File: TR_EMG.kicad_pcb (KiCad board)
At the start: 4 copper layers, 127 x 101.6 mm, 118 parts, among them J1 1727230, J2 1727230, J3 1844236, J4 MJ-3523-SMT-TR, J5 MJ-3523-SMT-TR, J6 MJ-3523-SMT-TR, J7 MJ-3523-SMT-TR, U1 ADS1115IDGSR, U101 INA115BU, U111 LT1169CS8-PBF, U112 LT1169CS8-PBF, U201 INA115BU, U211 LT1169CS8-PBF, U212 LT1169CS8-PBF, U301 INA115BU, U311 LT1169CS8-PBF, U312 LT1169CS8-PBF, U401 INA115BU, U411 LT1169CS8-PBF, U412 LT1169CS8-PBF

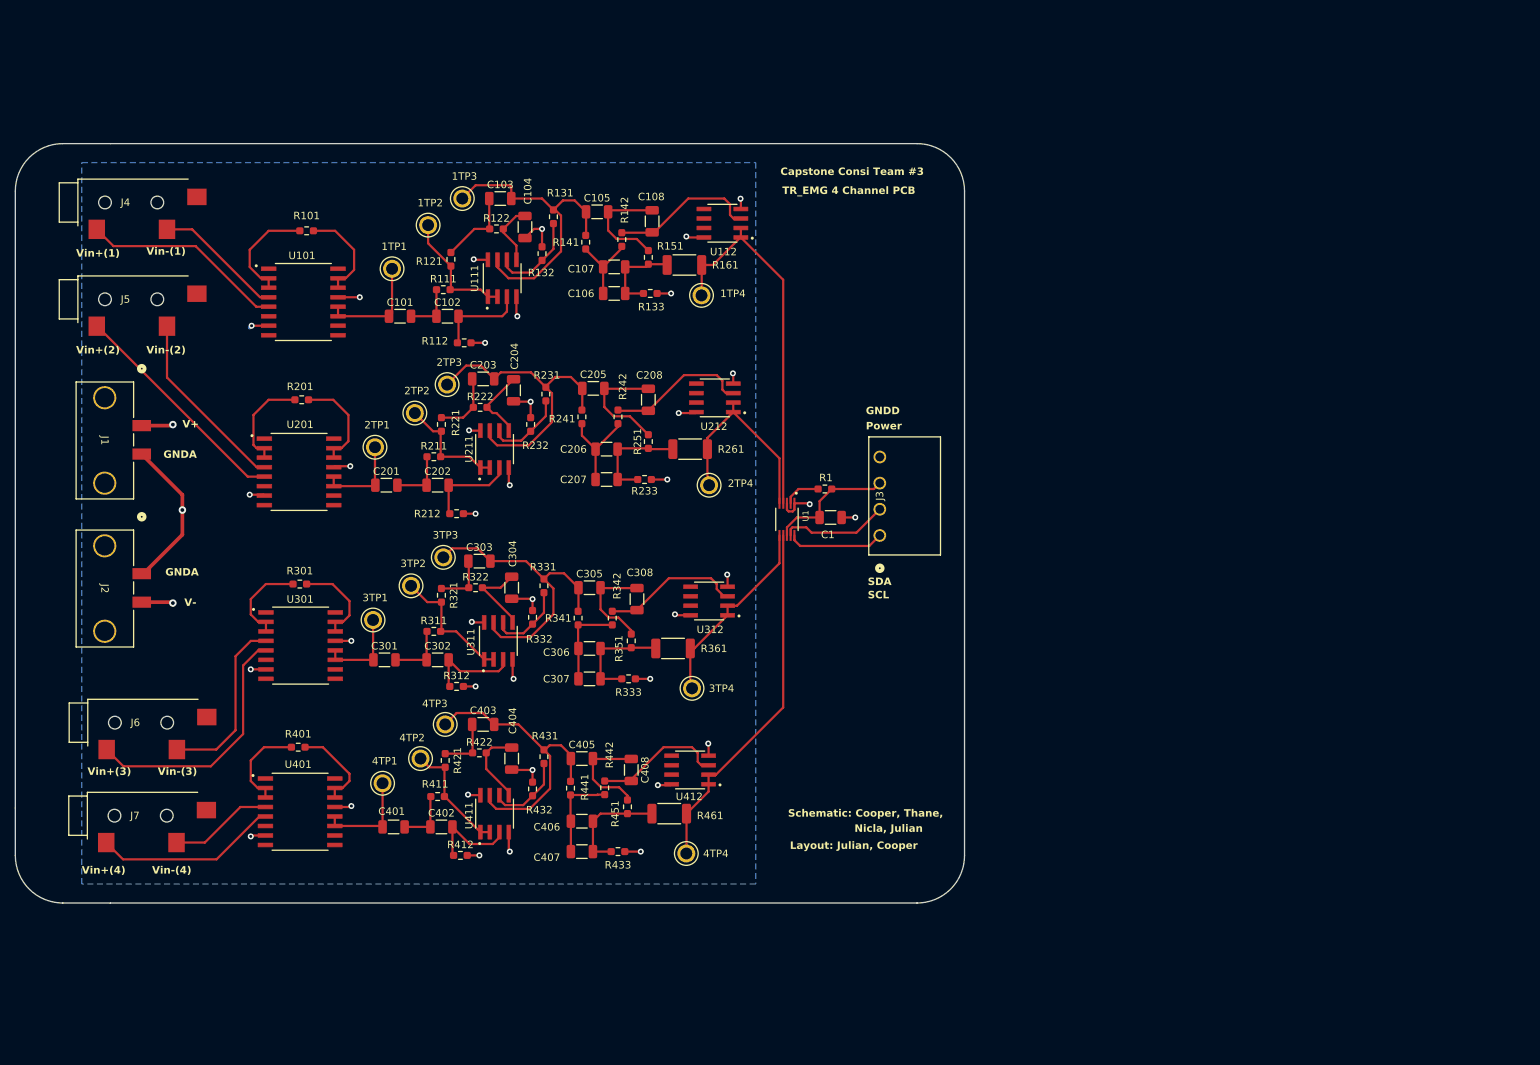
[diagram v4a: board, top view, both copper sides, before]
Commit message: Extended ground planes, rerouted some traces into vias. and pushed connectors to edge of board
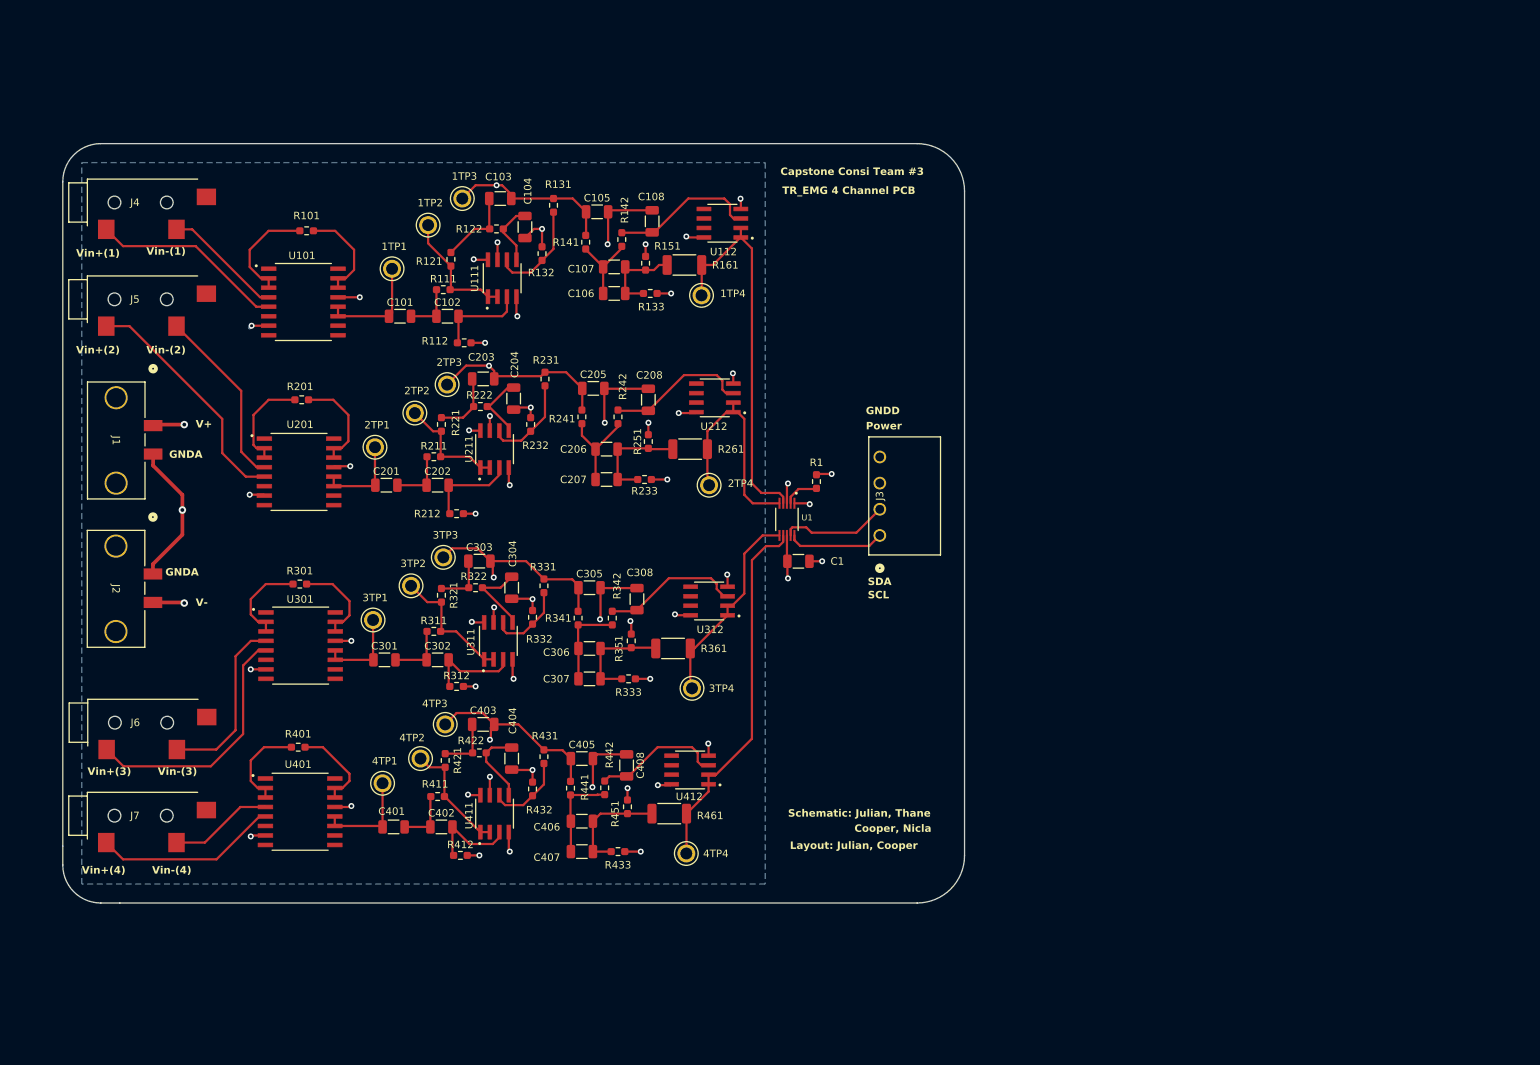
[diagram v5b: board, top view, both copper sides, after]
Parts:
- moved C1 7.27 mm to (187.3, 94.0)
- moved R231 2.02 mm to (153.4, 69.6)
- moved R131 1.53 mm to (154.6, 46.4)
- moved J1 1.52 mm to (101.0, 75.8)
- moved R1 1.51 mm to (189.7, 83.3), turned to -90 degrees
- moved J2 1.50 mm to (101.0, 95.7)
- moved J4 1.27 mm to (99.6, 46.0)
- moved J5 1.27 mm to (99.6, 58.9)
- moved C204 1.11 mm to (149.2, 72.2)
- moved C408 0.88 mm to (164.3, 121.3)
- moved R151 0.86 mm to (166.9, 54.1)
- moved R222 0.11 mm to (144.8, 73.3)
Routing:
- net /ADC/Power: track 17.2 -> 7.88 mm, vias 0 -> 2
- net /Filter1/2nd Band Pass Filter (5 - 500 Hz)/Vout: track 41.7 -> 32.4 mm, vias 0 -> 2
- net /Filter3/2nd Band Pass Filter (5 - 500 Hz)/Vout: track 40.5 -> 32.5 mm, vias 0 -> 2
- net /Filter2/2nd Band Pass Filter (5 - 500 Hz)/Vout: track 41.2 -> 33.4 mm, vias 0 -> 2
- net /Filter4/2nd Band Pass Filter (5 - 500 Hz)/Vout: track 40.0 -> 32.9 mm, vias 0 -> 2
- net /ADC/AIN1: track 27.3 -> 30.3 mm
- net Net-(C205-Pad2): track 15.8 -> 18.0 mm, vias 0 -> 2
- net Net-(C105-Pad2): track 15.0 -> 17.0 mm, vias 0 -> 2
- net Net-(U211--INB): track 10.6 -> 12.7 mm
- net GNDA: track 53.9 -> 51.9 mm
- net Net-(U111--INB): track 12.3 -> 13.8 mm
- net Net-(C305-Pad2): track 13.6 -> 15.1 mm, vias 0 -> 2
- net Vin+(2): track 30.8 -> 32.2 mm
- net /ADC/AIN0: track 50.0 -> 51.4 mm
- net Vin-(1): track 17.4 -> 16.1 mm
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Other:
- board size 127 x 101.6 mm -> 120.7 x 101.6 mm
- board text added: "Cooper, Nicla"
- board text added: "Schematic: Julian, Thane"
- board text removed: "Nicla, Julian"
- board text removed: "Schematic: Cooper, Thane,"

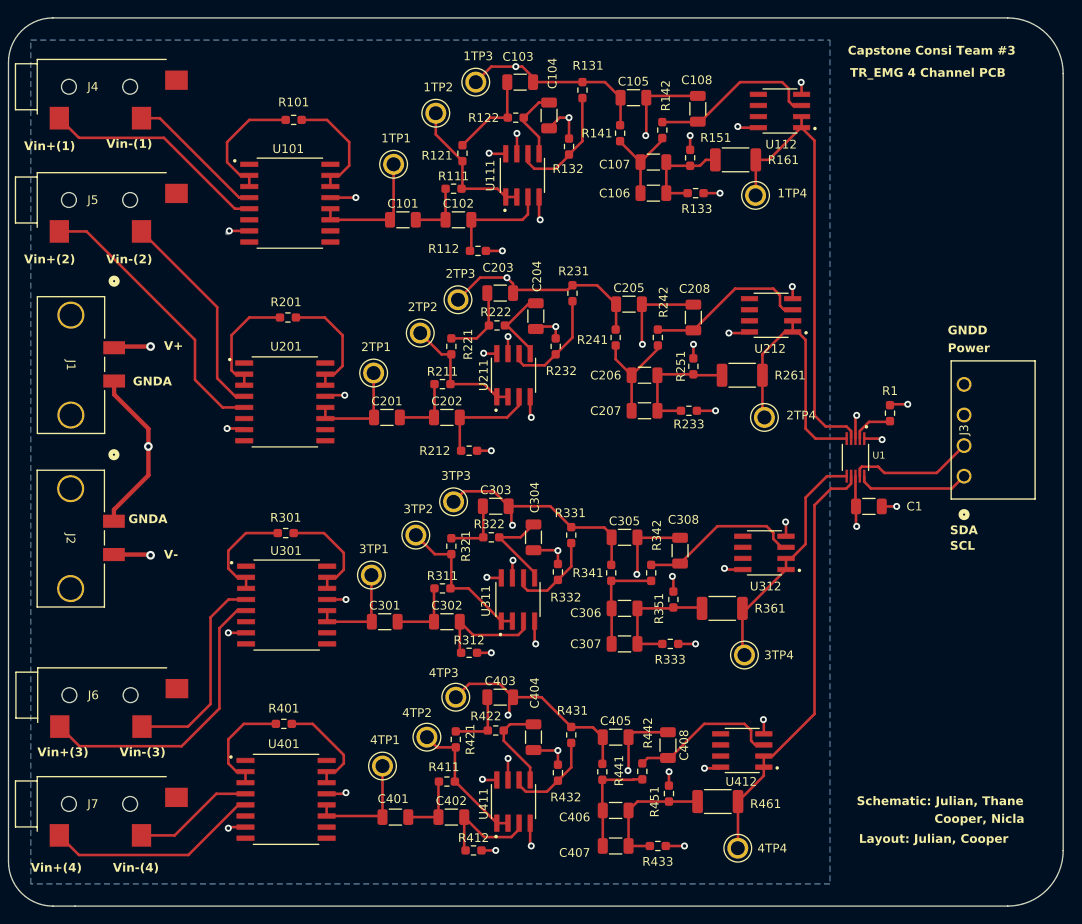
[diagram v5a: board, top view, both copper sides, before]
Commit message: Pushed adc connector to edge of pcb
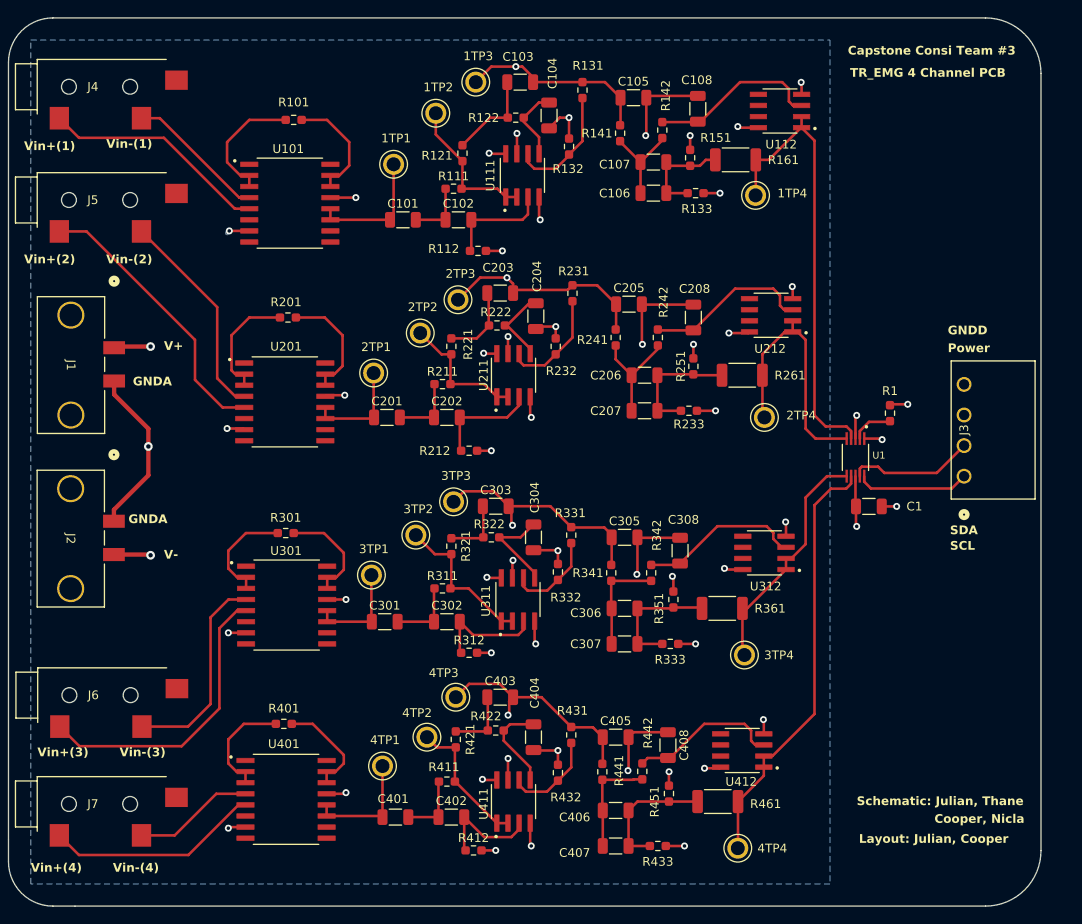
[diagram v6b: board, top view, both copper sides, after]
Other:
- board size 120.7 x 101.6 mm -> 118.1 x 101.6 mm
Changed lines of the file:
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@@
     )
   )
-  (gr_line (start 209.55 44.45) (end 209.55 133.35)
-    (stroke (width 0.1) (type default)) (layer "Edge.Cuts"))
-  (gr_arc (start 209.55 133.35) (mid 207.690128 137.840128) (end 203.2 139.7)
+  (gr_line (start 207.01 44.45) (end 207.01 133.35)
     (stroke (width 0.1) (type default)) (layer "Edge.Cuts"))
   (gr_arc (start 93.98 139.7) (mid 90.387898 138.212102) (end 88.9 134.62)
     (stroke (width 0.1) (type default)) (layer "Edge.Cuts"))
-  (gr_line (start 203.2 38.1) (end 93.98 38.1)
+  (gr_arc (start 200.66 38.1) (mid 205.150128 39.959872) (end 207.01 44.45)
+    (stroke (width 0.1) (type default)) (layer "Edge.Cuts"))
+  (gr_arc (start 207.01 133.35) (mid 205.150128 137.840128) (end 200.66 139.7)
+    (stroke (width 0.1) (type default)) (layer "Edge.Cuts"))
+  (gr_line (start 200.66 38.1) (end 93.98 38.1)
     (stroke (width 0.1) (type default)) (layer "Edge.Cuts"))
   (gr_line (start 96.52 139.7) (end 93.98 139.7)
@@
   (gr_line (start 88.9 132.08) (end 88.9 134.62)
     (stroke (width 0.1) (type default)) (layer "Edge.Cuts"))
-  (gr_arc (start 203.2 38.1) (mid 207.690128 39.959872) (end 209.55 44.45)
-    (stroke (width 0.1) (type default)) (layer "Edge.Cuts"))
   (gr_arc (start 88.9 43.18) (mid 90.387898 39.587898) (end 93.98 38.1)
     (stroke (width 0.1) (type default)) (layer "Edge.Cuts"))
-  (gr_line (start 203.2 139.7) (end 96.52 139.7)
+  (gr_line (start 200.66 139.7) (end 96.52 139.7)
     (stroke (width 0.1) (type default)) (layer "Edge.Cuts"))
   (gr_line (start 88.9 43.18) (end 88.9 132.08)
@@
     (polygon
       (pts
-        (xy 206.756 74.676)
-        (xy 206.756 97.536)
+        (xy 204.216 74.676)
+        (xy 204.216 97.536)
         (xy 184.404 97.536)
         (xy 184.404 74.676)
@@
       (pts
         (xy 184.404 74.676)
-        (xy 206.756 74.676)
-        (xy 206.756 97.536)
+        (xy 204.216 74.676)
+        (xy 204.216 97.536)
         (xy 184.404 97.536)
       )

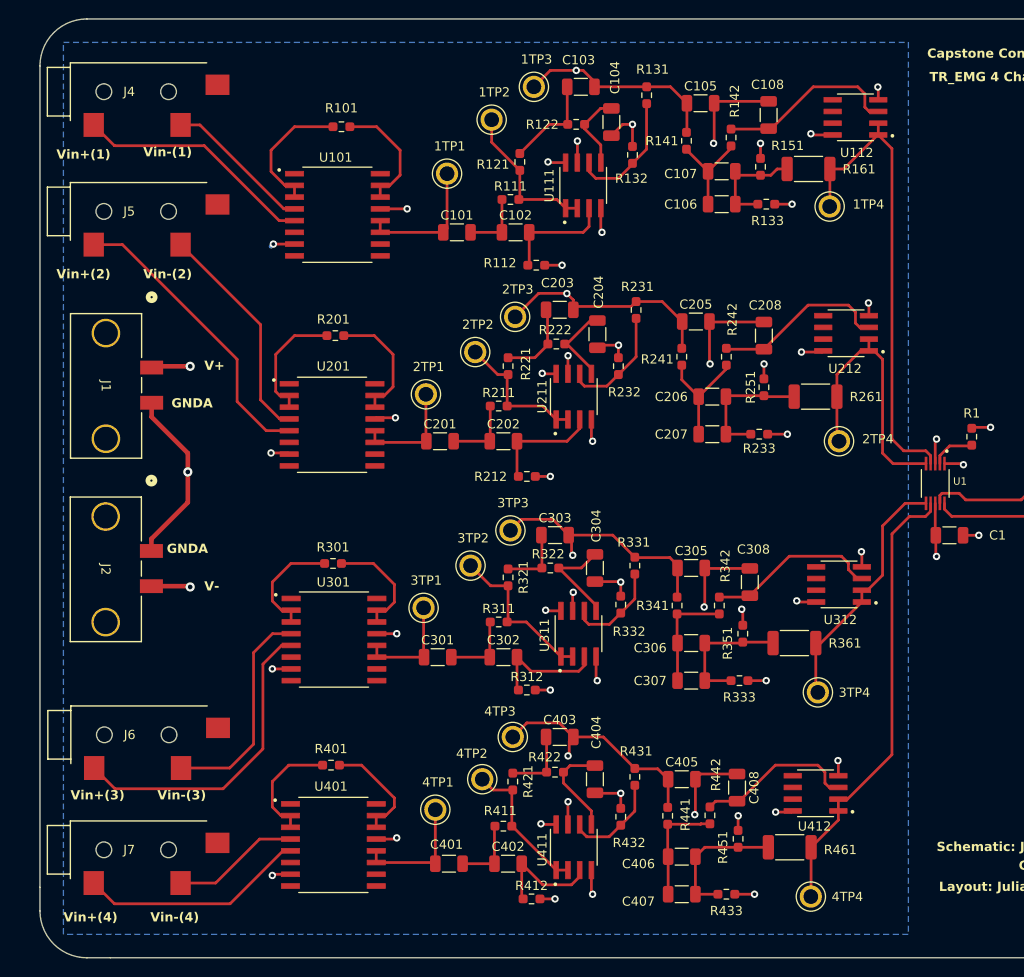
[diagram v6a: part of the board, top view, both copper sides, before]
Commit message: ToTheEdge,LCSCNums
Moved the 3.5mm connectors to the edge and edited their footprint courtyard so no errors. Adjusted the planes so that it bordered 3.5mm connector pads well and didn't go to edge cuts. Added LCSC part numbers to the parts that were in stock.
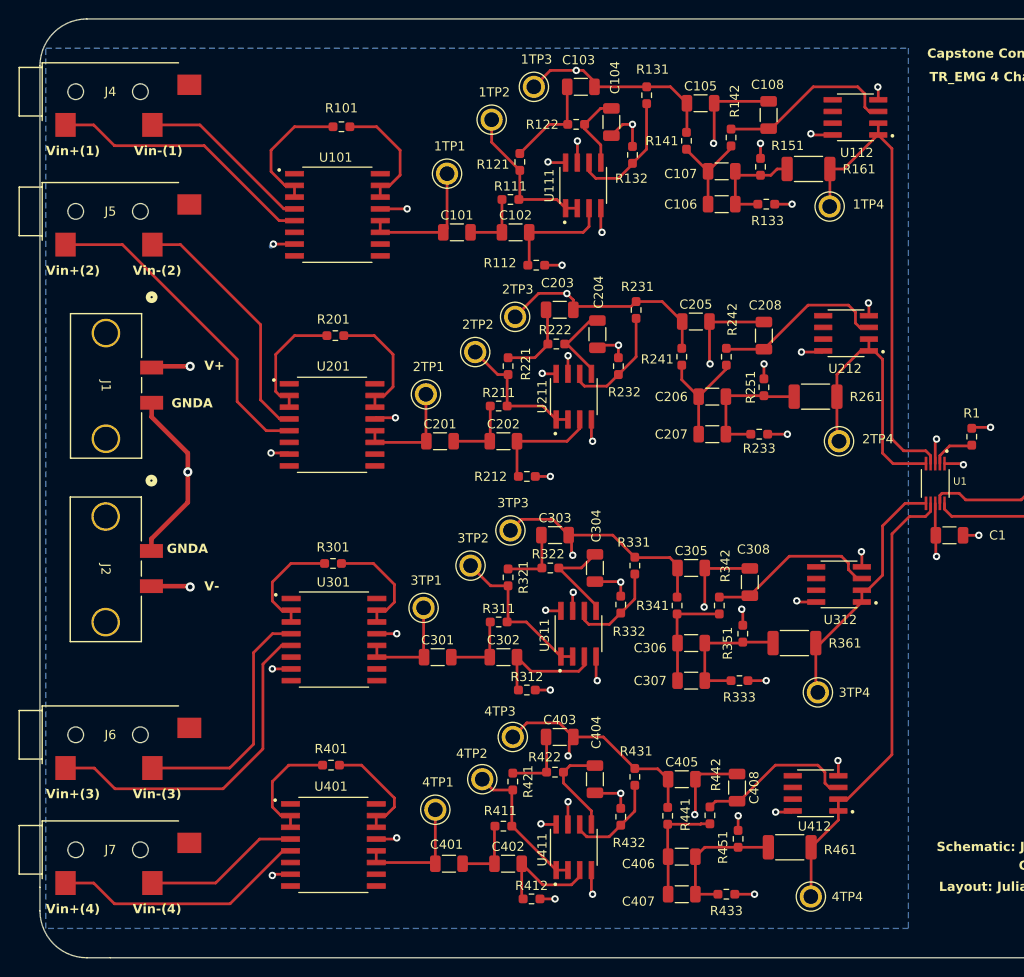
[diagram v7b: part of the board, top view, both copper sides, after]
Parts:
- J4, J5, J6, J7: footprint footprints:CONN_MJ-3523_CUD -> footprints:CONN_MJ-3523_CUD_CtYrd
- moved J6 3.10 mm to (96.5, 115.6)
- moved J4 3.05 mm to (96.5, 46.0)
- moved J5 3.05 mm to (96.5, 58.9)
- moved J7 3.05 mm to (96.5, 128.0)
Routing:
- net Vin+(3): track 34.0 -> 37.1 mm
- net Vin-(3): track 23.7 -> 26.8 mm
- net Vin-(4): track 14.0 -> 17.0 mm
- net Vin-(2): track 24.3 -> 27.4 mm
- net Vin-(1): track 16.1 -> 19.1 mm
- net Vin+(4): track 24.6 -> 27.6 mm
- net Vin+(2): track 32.2 -> 35.2 mm
- net Vin+(1): track 26.0 -> 29.1 mm
